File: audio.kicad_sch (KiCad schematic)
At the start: 9 parts, among them J4 Conn_01x02, U5 MAX98357A

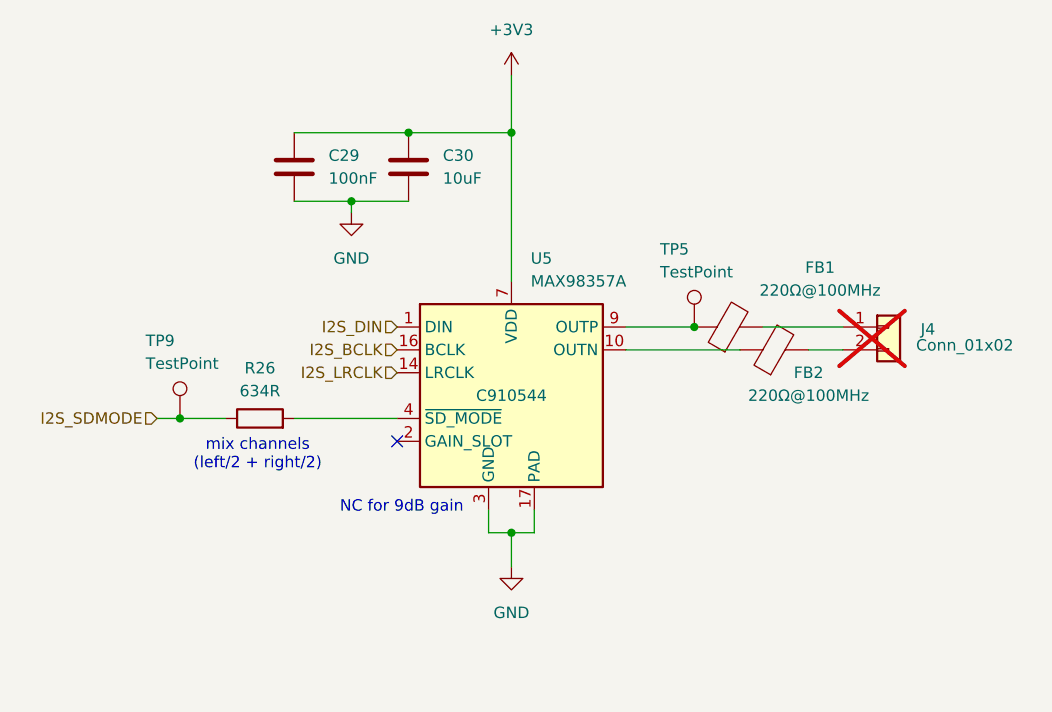
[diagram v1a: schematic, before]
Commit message: fix bom, add pulldown on amp
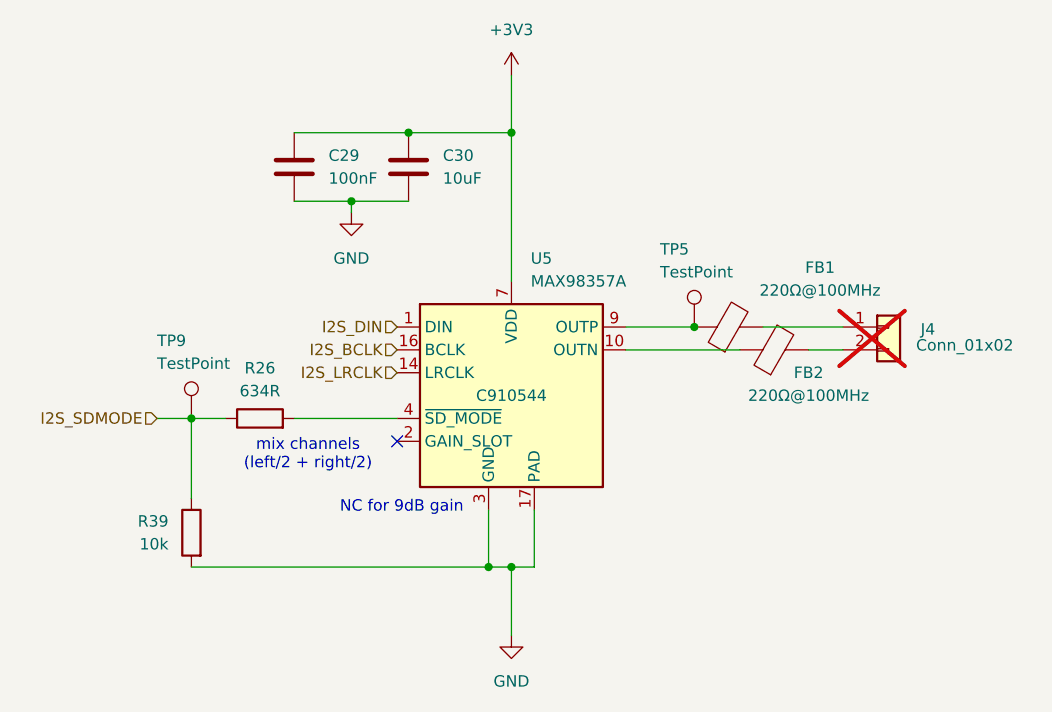
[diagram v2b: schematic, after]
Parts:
- added R39: 10k, Resistor_SMD:R_0603_1608Metric, symbol Device:R
- R26: LCSC (none) -> C245990
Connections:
- net GND: now also R39.2
- net I2S_SDMODE: now also R39.1
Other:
- moved on the sheet: TP9
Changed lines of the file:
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@@
 	(text "mix channels \n(left/2 + right/2)"
 		(exclude_from_sim no)
-		(at 105.156 105.664 0)
+		(at 110.744 105.664 0)
 		(effects
 			(font
@@
 	)
 	(junction
-		(at 96.52 101.6)
+		(at 133.35 118.11)
+		(diameter 0)
+		(color 0 0 0 0)
+	)
+	(junction
+		(at 97.79 101.6)
 		(diameter 0)
 		(color 0 0 0 0)
@@
 	)
 	(junction
-		(at 133.35 114.3)
+		(at 130.81 118.11)
 		(diameter 0)
 		(color 0 0 0 0)
@@
 	(wire
 		(pts
-			(xy 130.81 111.76) (xy 130.81 114.3)
+			(xy 130.81 111.76) (xy 130.81 118.11)
 		)
 		(stroke
@@
 	(wire
 		(pts
-			(xy 130.81 114.3) (xy 133.35 114.3)
-		)
-		(stroke
-			(width 0)
-			(type default)
-		)
-	)
-	(wire
-		(pts
-			(xy 93.98 101.6) (xy 96.52 101.6)
-		)
-		(stroke
-			(width 0)
-			(type default)
-		)
-	)
-	(wire
-		(pts
-			(xy 133.35 114.3) (xy 133.35 118.11)
+			(xy 130.81 118.11) (xy 133.35 118.11)
+		)
+		(stroke
+			(width 0)
+			(type default)
+		)
+	)
+	(wire
+		(pts
+			(xy 93.98 101.6) (xy 97.79 101.6)
 		)
 		(stroke
@@
 	(wire
 		(pts
-			(xy 96.52 101.6) (xy 101.6 101.6)
+			(xy 133.35 118.11) (xy 133.35 125.73)
+		)
+		(stroke
+			(width 0)
+			(type default)
+		)
+	)
+	(wire
+		(pts
+			(xy 97.79 101.6) (xy 101.6 101.6)
+		)
+		(stroke
+			(width 0)
+			(type default)
+		)
+	)
+	(wire
+		(pts
+			(xy 97.79 118.11) (xy 130.81 118.11)
 		)
 		(stroke
@@
 	(wire
 		(pts
-			(xy 135.89 114.3) (xy 135.89 111.76)
+			(xy 97.79 101.6) (xy 97.79 110.49)
+		)
+		(stroke
+			(width 0)
+			(type default)
+		)
+	)
+	(wire
+		(pts
+			(xy 135.89 118.11) (xy 135.89 111.76)
 		)
 		(stroke
@@
 	(wire
 		(pts
-			(xy 133.35 114.3) (xy 135.89 114.3)
+			(xy 133.35 118.11) (xy 135.89 118.11)
 		)
 		(stroke
@@
 	)
 	(symbol
+		(lib_id "Device:R")
+		(at 97.79 114.3 0)
+		(mirror y)
+		(unit 1)
+		(body_style 1)
+		(exclude_from_sim no)
+		(in_bom yes)
+		(on_board yes)
+		(in_pos_files yes)
+		(dnp no)
+		(fields_autoplaced yes)
+		(property "Reference" "R39"
+			(at 95.25 113.0299 0)
+			(show_name no)
+			(do_not_autoplace no)
+			(effects
+				(font
+					(size 1.27 1.27)
+				)
+				(justify left)
+			)
+		)
+		(property "Value" "10k"
+			(at 95.25 115.5699 0)
+			(show_name no)
+			(do_not_autoplace no)
+			(effects
+				(font
+					(size 1.27 1.27)
+				)
+				(justify left)
+			)
+		)
+		(property "Footprint" "Resistor_SMD:R_0603_1608Metric"
+			(at 99.568 114.3 90)
+			(hide yes)
+			(show_name no)
+			(do_not_autoplace no)
+			(effects
+				(font
+					(size 1.27 1.27)
+				)
+			)
+		)
+		(property "Datasheet" ""
+			(at 97.79 114.3 0)
+			(hide yes)
+			(show_name no)
+			(do_not_autoplace no)
+			(effects
+				(font
+					(size 1.27 1.27)
+				)
+			)
+		)
+		(property "Description" "Resistor"
+			(at 97.79 114.3 0)
+			(hide yes)
+			(show_name no)
+			(do_not_autoplace no)
+			(effects
+				(font
+					(size 1.27 1.27)
+				)
+			)
+		)
+		(property "LCSC" ""
+			(at 97.79 114.3 0)
+			(hide yes)
+			(show_name no)
+			(do_not_autoplace no)
+			(effects
+				(font
+					(size 1.27 1.27)
+				)
+			)
+		)
+		(property "Manufacturer" ""
+			(at 97.79 114.3 0)
+			(hide yes)
+			(show_name no)
+			(do_not_autoplace no)
+			(effects
+				(font
+					(size 1.27 1.27)
+				)
+			)
+		)
+		(property "Manufacturer Part Number" ""
+			(at 97.79 114.3 0)
+			(hide yes)
+			(show_name no)
+			(do_not_autoplace no)
+			(effects
+				(font
+					(size 1.27 1.27)
+				)
+			)
+		)
+		(pin "1"
+		)
+		(pin "2"
+		)
+		(instances
+			(project "gameboy"
+				(path "/f4643692-c319-40a7-82a2-3e775c0a417f/544a4a01-8cf8-45b3-bce5-8d02a4ea8581"
+					(reference "R39")
+					(unit 1)
+				)
+			)
+		)
+	)
+	(symbol
 		(lib_id "Connector:TestPoint")
-		(at 96.52 101.6 0)
+		(at 97.79 101.6 0)
 		(unit 1)
 		(body_style 1)
@@
 		(in_bom no)
 		(on_board yes)
-		(in_pos_files yes)
+		(in_pos_files no)
 		(dnp no)
 		(property "Reference" "TP9"
-			(at 92.71 92.964 0)
+			(at 93.98 92.964 0)
 			(show_name no)
 			(do_not_autoplace no)
@@
 		)
 		(property "Value" "TestPoint"
-			(at 92.71 95.504 0)
+			(at 93.98 95.504 0)
 			(show_name no)
 			(do_not_autoplace no)
@@
 		)
 		(property "Footprint" "TestPoint:TestPoint_Pad_D1.0mm"
-			(at 101.6 101.6 0)
+			(at 102.87 101.6 0)
 			(hide yes)
 			(show_name no)
@@
 		)
 		(property "Datasheet" ""
-			(at 101.6 101.6 0)
+			(at 102.87 101.6 0)
 			(hide yes)
 			(show_name no)
@@
 		)
 		(property "Description" "test point"
-			(at 96.52 101.6 0)
+			(at 97.79 101.6 0)
 			(hide yes)
 			(show_name no)
@@
 		)
 		(property "LCSC" ""
-			(at 96.52 101.6 0)
+			(at 97.79 101.6 0)
 			(hide yes)
 			(show_name no)
@@
 		)
 		(property "Manufacturer" ""
-			(at 96.52 101.6 0)
+			(at 97.79 101.6 0)
 			(hide yes)
 			(show_name no)
@@
 		)
 		(property "Manufacturer Part Number" ""
-			(at 96.52 101.6 0)
+			(at 97.79 101.6 0)
 			(hide yes)
 			(show_name no)
@@
 	(symbol
 		(lib_id "power:GND")
-		(at 133.35 118.11 0)
+		(at 133.35 125.73 0)
 		(unit 1)
 		(body_style 1)
@@
 		(fields_autoplaced yes)
 		(property "Reference" "#PWR032"
-			(at 133.35 124.46 0)
+			(at 133.35 132.08 0)
 			(hide yes)
 			(show_name no)
@@
 		)
 		(property "Value" "GND"
-			(at 133.35 123.19 0)
+			(at 133.35 130.81 0)
 			(show_name no)
 			(do_not_autoplace no)
@@
 		)
 		(property "Footprint" ""
-			(at 133.35 118.11 0)
+			(at 133.35 125.73 0)
 			(hide yes)
 			(show_name no)
@@
 		)
 		(property "Datasheet" ""
-			(at 133.35 118.11 0)
+			(at 133.35 125.73 0)
 			(hide yes)
 			(show_name no)
@@
 		)
 		(property "Description" "Power symbol creates a global label with name \"GND\" , ground"
-			(at 133.35 118.11 0)
+			(at 133.35 125.73 0)
 			(hide yes)
 			(show_name no)
@@
 		(in_bom no)
 		(on_board yes)
-		(in_pos_files yes)
+		(in_pos_files no)
 		(dnp no)
 		(property "Reference" "TP5"
@@
 			)
 		)
-		(property "LCSC" ""
+		(property "LCSC" "C245990"
 			(at 105.41 101.6 0)
 			(hide yes)

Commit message: changed amp sd_mode resistor value, move caps, add i2c pullups
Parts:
- R26: value 634R -> 634k; LCSC C245990 -> C2999499
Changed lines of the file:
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@@
 			)
 		)
-		(property "Value" "634R"
+		(property "Value" "634k"
 			(at 105.41 98.552 90)
 			(show_name no)
@@
 			)
 		)
-		(property "LCSC" "C245990"
+		(property "LCSC" "C2999499"
 			(at 105.41 101.6 0)
 			(hide yes)
